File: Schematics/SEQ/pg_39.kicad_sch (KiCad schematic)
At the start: 14 parts

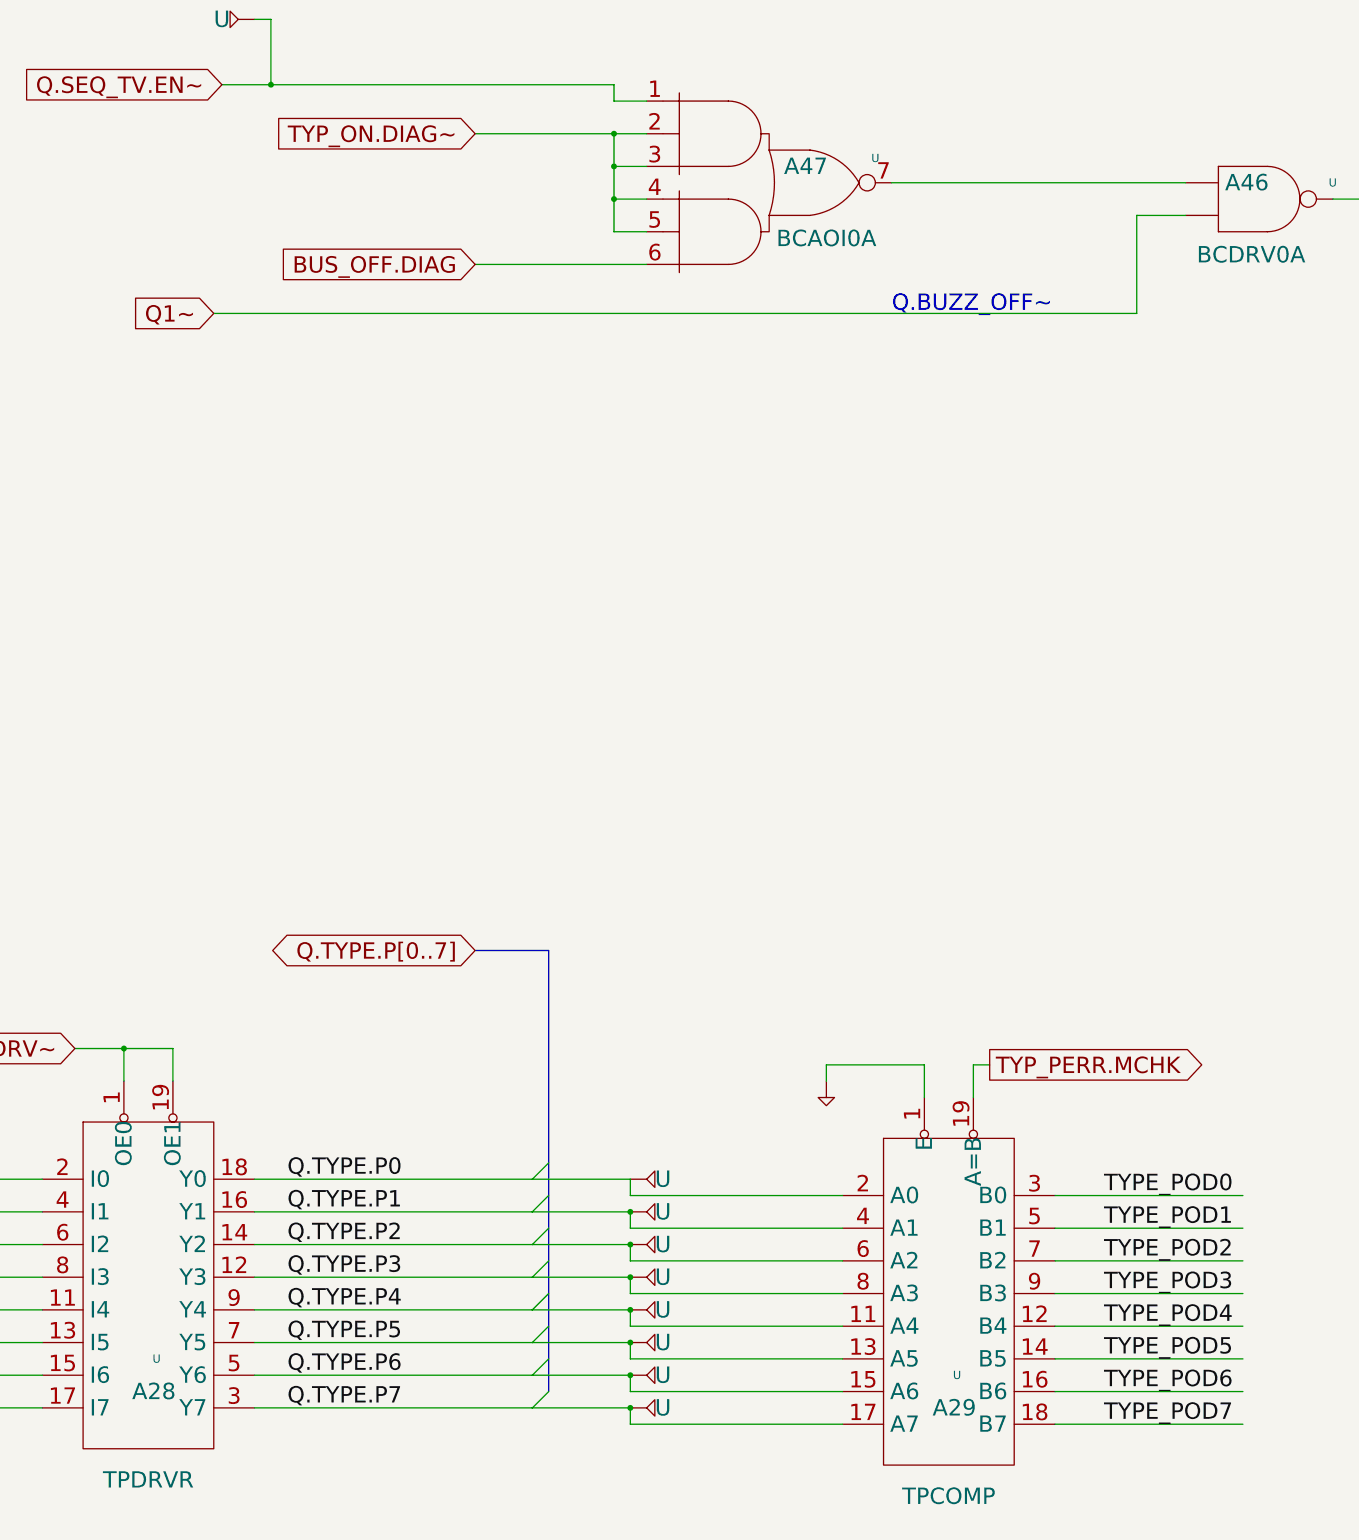
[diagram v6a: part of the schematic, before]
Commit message: Fix WCS parity
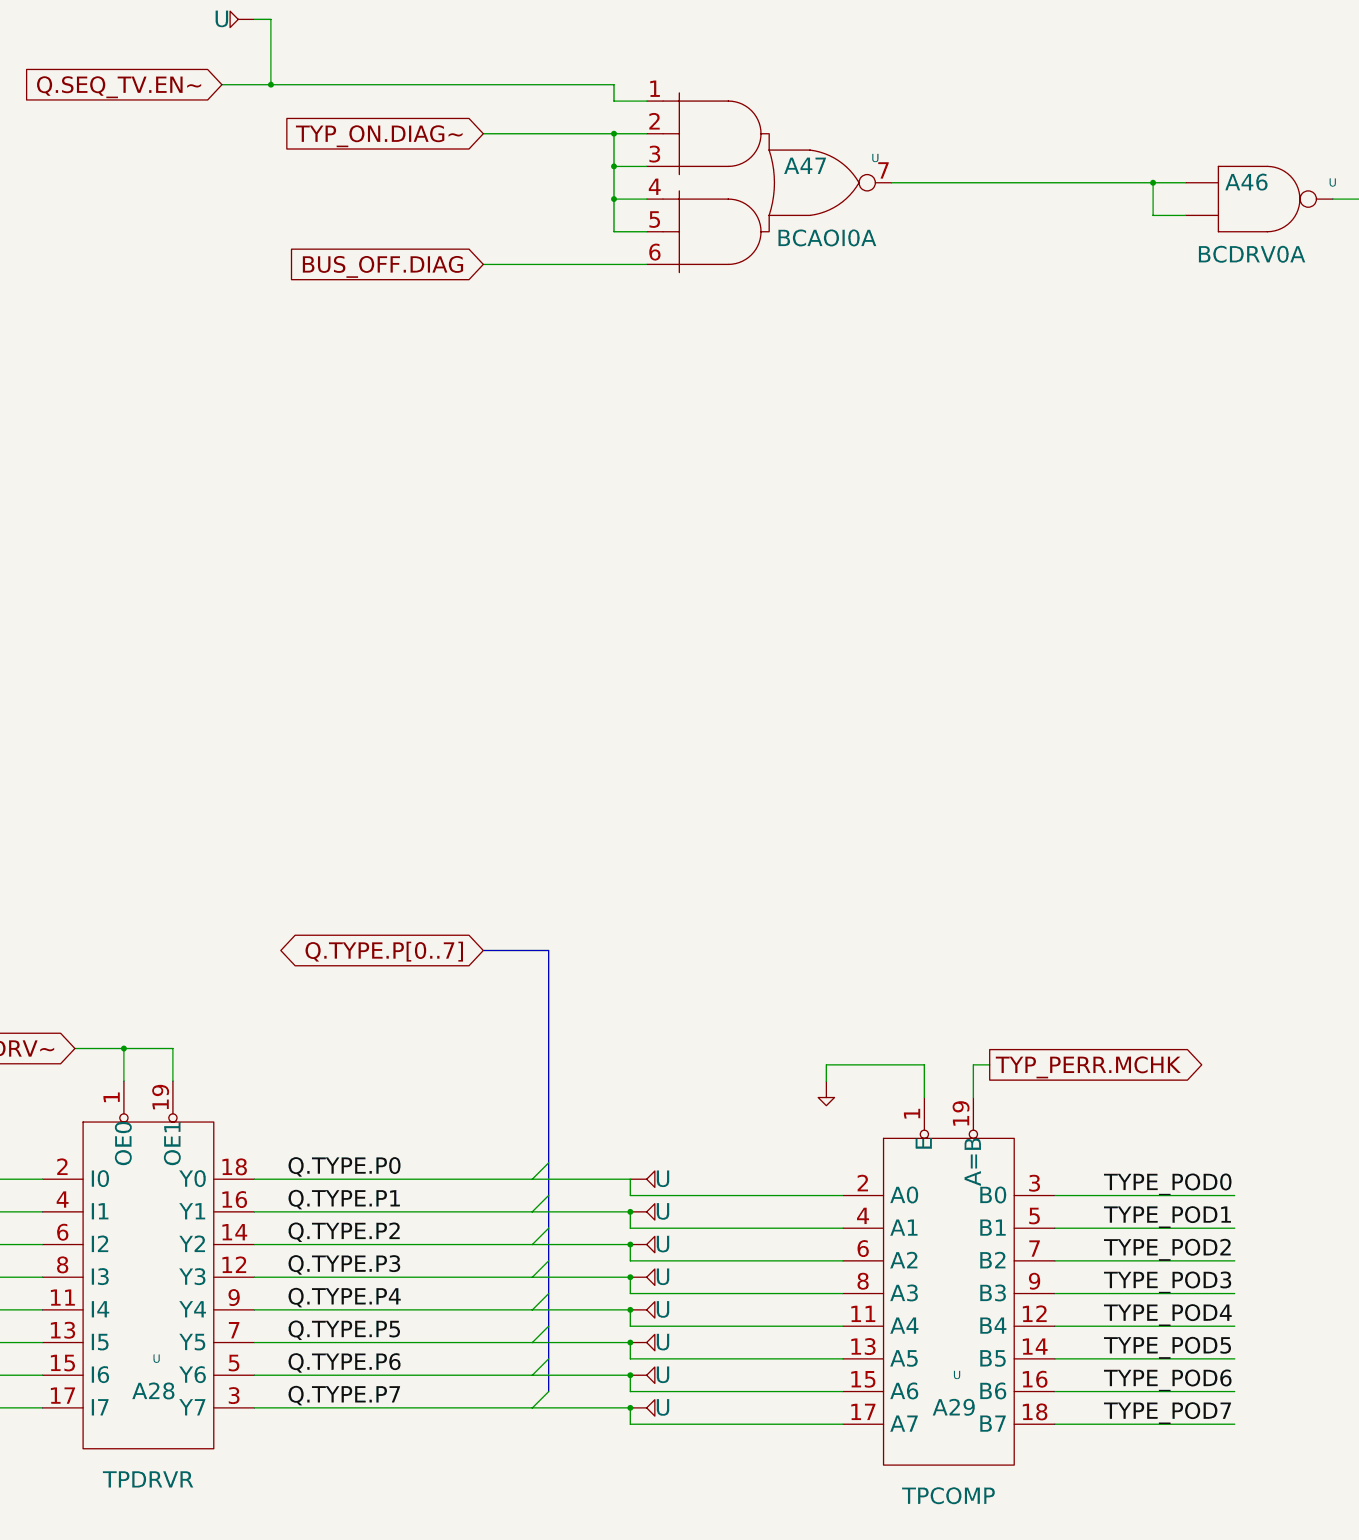
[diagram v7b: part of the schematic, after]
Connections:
- net Q1~ is gone; now on an unnamed net: U.2 (D1)
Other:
- note removed: "Q.BUZZ_OFF~"
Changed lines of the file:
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@@
   (junction (at 279.4 294.64) (diameter 0) (color 0 0 0 0)
+  )
+  (junction (at 439.42 160.02) (diameter 0) (color 0 0 0 0)
   )
   (junction (at 358.14 335.28) (diameter 0) (color 0 0 0 0)
@@
     (stroke (width 0) (type default))
   )
+  (wire (pts (xy 439.42 160.02) (xy 444.5 160.02))
+    (stroke (width 0) (type default))
+  )
   (wire (pts (xy 175.26 45.72) (xy 205.74 45.72))
     (stroke (width 0) (type default))
@@
     (stroke (width 0) (type default))
   )
-  (wire (pts (xy 293.37 180.34) (xy 436.88 180.34))
-    (stroke (width 0) (type default))
-  )
   (bus (pts (xy 106.68 93.98) (xy 106.68 99.06))
     (stroke (width 0) (type default))
@@
     (stroke (width 0) (type default))
   )
-  (wire (pts (xy 424.18 342.9) (xy 453.39 342.9))
+  (wire (pts (xy 424.18 342.9) (xy 452.12 342.9))
     (stroke (width 0) (type default))
   )
@@
     (stroke (width 0) (type default))
   )
-  (wire (pts (xy 398.78 160.02) (xy 444.5 160.02))
-    (stroke (width 0) (type default))
-  )
-  (wire (pts (xy 334.01 172.72) (xy 360.68 172.72))
+  (wire (pts (xy 398.78 160.02) (xy 439.42 160.02))
+    (stroke (width 0) (type default))
+  )
+  (wire (pts (xy 335.28 172.72) (xy 360.68 172.72))
     (stroke (width 0) (type default))
   )
@@
     (stroke (width 0) (type default))
   )
-  (wire (pts (xy 424.18 347.98) (xy 453.39 347.98))
+  (wire (pts (xy 424.18 347.98) (xy 452.12 347.98))
     (stroke (width 0) (type default))
   )
@@
     (stroke (width 0) (type default))
   )
-  (wire (pts (xy 424.18 337.82) (xy 453.39 337.82))
+  (wire (pts (xy 424.18 337.82) (xy 452.12 337.82))
     (stroke (width 0) (type default))
   )
@@
     (stroke (width 0) (type default))
   )
-  (wire (pts (xy 334.01 152.4) (xy 355.6 152.4))
+  (wire (pts (xy 335.28 152.4) (xy 355.6 152.4))
     (stroke (width 0) (type default))
   )
@@
     (stroke (width 0) (type default))
   )
-  (wire (pts (xy 424.18 332.74) (xy 453.39 332.74))
+  (wire (pts (xy 424.18 332.74) (xy 452.12 332.74))
     (stroke (width 0) (type default))
   )
@@
     (stroke (width 0) (type default))
   )
-  (wire (pts (xy 424.18 322.58) (xy 453.39 322.58))
+  (wire (pts (xy 424.18 322.58) (xy 452.12 322.58))
     (stroke (width 0) (type default))
   )
@@
     (stroke (width 0) (type default))
   )
-  (wire (pts (xy 424.18 317.5) (xy 453.39 317.5))
-    (stroke (width 0) (type default))
-  )
-  (wire (pts (xy 436.88 180.34) (xy 436.88 165.1))
+  (wire (pts (xy 424.18 317.5) (xy 452.12 317.5))
     (stroke (width 0) (type default))
   )
@@
     (stroke (width 0) (type default))
   )
+  (wire (pts (xy 439.42 165.1) (xy 439.42 160.02))
+    (stroke (width 0) (type default))
+  )
   (bus (pts (xy 106.68 302.26) (xy 106.68 307.34))
     (stroke (width 0) (type default))
@@
     (stroke (width 0) (type default))
   )
-  (wire (pts (xy 424.18 327.66) (xy 453.39 327.66))
+  (wire (pts (xy 424.18 327.66) (xy 452.12 327.66))
     (stroke (width 0) (type default))
   )
@@
     (stroke (width 0) (type default))
   )
-  (wire (pts (xy 436.88 165.1) (xy 444.5 165.1))
-    (stroke (width 0) (type default))
-  )
   (wire (pts (xy 134.62 142.24) (xy 109.22 142.24))
     (stroke (width 0) (type default))
@@
     (stroke (width 0) (type default))
   )
-  (wire (pts (xy 424.18 353.06) (xy 453.39 353.06))
+  (wire (pts (xy 424.18 353.06) (xy 452.12 353.06))
     (stroke (width 0) (type default))
   )
@@
     (stroke (width 0) (type default))
   )
+  (wire (pts (xy 444.5 165.1) (xy 439.42 165.1))
+    (stroke (width 0) (type default))
+  )
   (wire (pts (xy 134.62 294.64) (xy 109.22 294.64))
     (stroke (width 0) (type default))
@@
     (stroke (width 0) (type default))
   )
-  (bus (pts (xy 334.01 279.4) (xy 345.44 279.4))
+  (bus (pts (xy 335.28 279.4) (xy 345.44 279.4))
     (stroke (width 0) (type default))
   )
@@
     (stroke (width 0) (type default))
   )
-  (text "Q.BUZZ_OFF~" (at 398.78 180.34 0)
-    (effects (font (size 2.54 2.54)) (justify left bottom))
-  )
   (label "TYPE~53" (at 114.3 304.8 0) (fields_autoplaced)
     (effects (font (size 2.54 2.54)) (justify left bottom))
@@
     (effects (font (size 2.54 2.54)) (justify left bottom))
   )
-  (global_label "BUS_OFF.DIAG" (shape input) (at 334.01 172.72 180) (fields_autoplaced)
+  (global_label "BUS_OFF.DIAG" (shape input) (at 335.28 172.72 180) (fields_autoplaced)
     (effects (font (size 2.54 2.54)) (justify right))
-    (property "Intersheet References" "${INTERSHEET_REFS}" (id 0) (at 302.9373 172.5613 0)
+    (property "Intersheet References" "${INTERSHEET_REFS}" (id 0) (at 304.2073 172.5613 0)
       (effects (font (size 1.905 1.905)) (justify right))
     )
@@
     )
   )
-  (global_label "Q1~" (shape input) (at 293.37 180.34 180) (fields_autoplaced)
-    (effects (font (size 2.54 2.54)) (justify right))
-    (property "Intersheet References" "${INTERSHEET_REFS}" (id 0) (at 280.7923 180.34 0)
-      (effects (font (size 1.905 1.905)) (justify right))
-    )
-  )
   (global_label "TYPE_DRV~" (shape input) (at 271.78 294.64 180) (fields_autoplaced)
     (effects (font (size 2.54 2.54)) (justify right))
@@
     )
   )
-  (global_label "Q.TYPE.P[0..7]" (shape bidirectional) (at 334.01 279.4 180) (fields_autoplaced)
+  (global_label "Q.TYPE.P[0..7]" (shape bidirectional) (at 335.28 279.4 180) (fields_autoplaced)
     (effects (font (size 2.54 2.54)) (justify right))
-    (property "Intersheet References" "${INTERSHEET_REFS}" (id 0) (at 301.9697 279.2413 0)
+    (property "Intersheet References" "${INTERSHEET_REFS}" (id 0) (at 303.2397 279.2413 0)
       (effects (font (size 1.905 1.905)) (justify right))
     )
   )
-  (global_label "TYP_ON.DIAG~" (shape input) (at 334.01 152.4 180) (fields_autoplaced)
+  (global_label "TYP_ON.DIAG~" (shape input) (at 335.28 152.4 180) (fields_autoplaced)
     (effects (font (size 2.54 2.54)) (justify right))
-    (property "Intersheet References" "${INTERSHEET_REFS}" (id 0) (at 303.784 152.2413 0)
+    (property "Intersheet References" "${INTERSHEET_REFS}" (id 0) (at 305.054 152.2413 0)
       (effects (font (size 1.905 1.905)) (justify right))
     )
